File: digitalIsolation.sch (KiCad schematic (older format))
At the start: 6 parts, among them U14 74AHC1G14, U15 Si8651

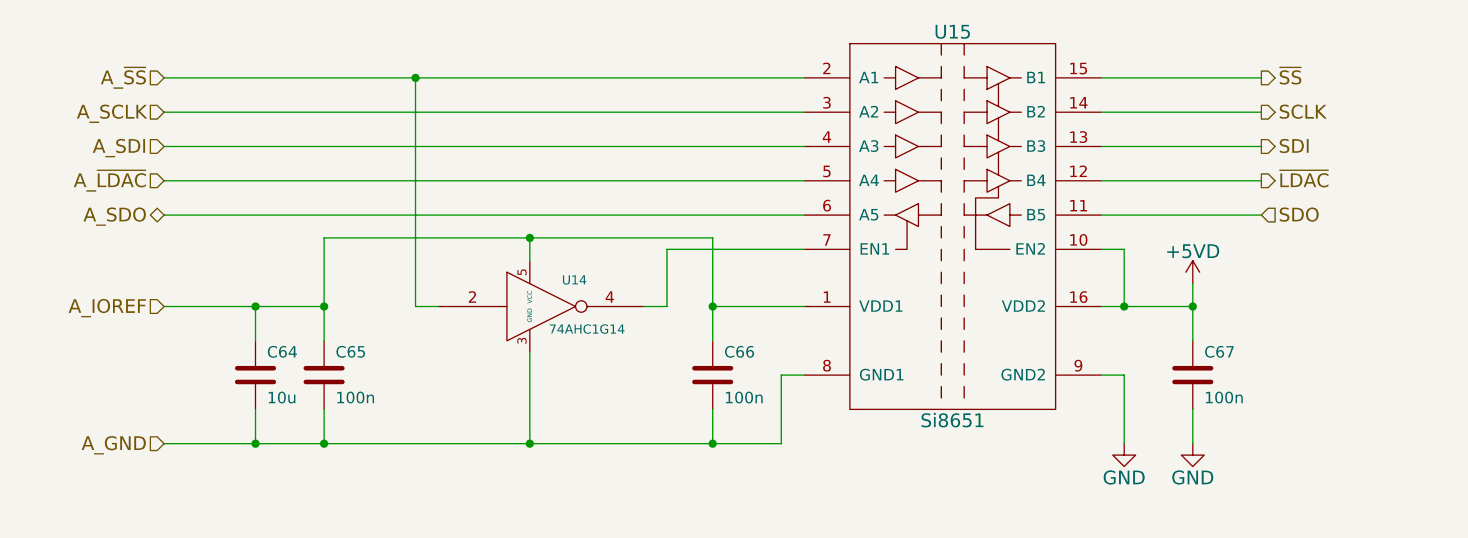
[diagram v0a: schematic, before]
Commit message: Updated all part descriptions
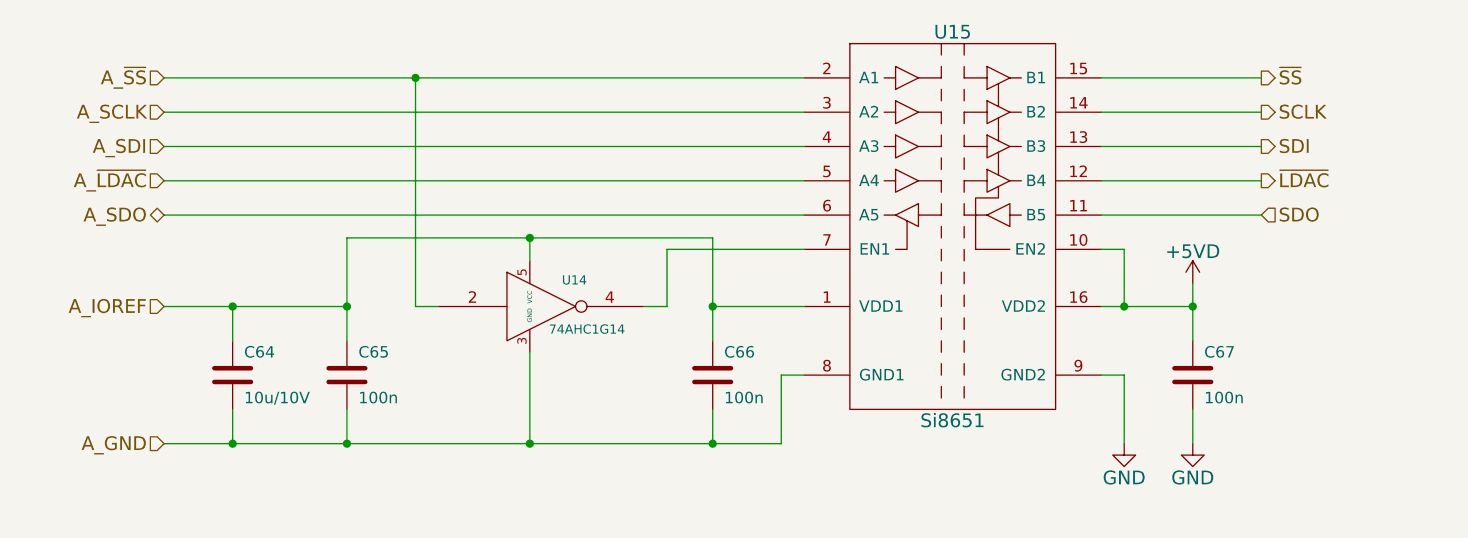
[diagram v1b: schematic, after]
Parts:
- C64: value 10u -> 10u/10V; Alt. Order Code (none) -> 81-GRM21BR61A106KE19; Alt. Supplier (none) -> Mouser; Note (none) -> 10μ/10V X5R 0805 ceramic capacitor; Package (none) -> 0805; Supplier (none) -> Farnell
- C65, C66, C67: Alt. Order Code (none) -> 710-885012206095; Alt. Supplier (none) -> Mouser; Note (none) -> 100n/50V X7R 0603 ceramic capacitor; Package (none) -> 0603; Supplier (none) -> Farnell
- U14: Alt. Order Code (none) -> 595-SN74AHC1G14DCKR; Alt. Supplier (none) -> Mouser; Note (none) -> Single Schmitt trigger inverter; Package (none) -> SC-70-5; Supplier (none) -> Farnell
- U15: Alt. Order Code (none) -> 634-SI8651EC-B-IS1; Alt. Supplier (none) -> Mouser; Note (none) -> Digital isolators 5 channel 3.75kV 8ns 4/1; Package (none) -> SOIC-16; Supplier (none) -> Farnell
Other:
- moved on the sheet: C64, C65
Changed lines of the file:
@@
 EESchema Schematic File Version 2
-LIBS:MicroFLiC_DAC_1_0-rescue
 LIBS:power
 LIBS:device
@@
 LIBS:valves
 LIBS:jakub
-LIBS:MicroFLiC_DAC_1_0-cache
+LIBS:MicroFLiC_DAC-cache
 EELAYER 25 0
 EELAYER END
@@
 F 4 "SI8651EC-B-IS1" H 7050 2850 60  0001 C CNN "Part Number"
 F 5 "Silicon Labs" H 7050 2850 60  0001 C CNN "Manufacturer"
-F 6 "2423323" H 7050 2850 60  0001 C CNN "Order Code"
+F 6 "SOIC-16" H 7050 2850 60  0001 C CNN "Package"
+F 7 "Farnell" H 7050 2850 60  0001 C CNN "Supplier"
+F 8 "2423323" H 7050 2850 60  0001 C CNN "Order Code"
+F 9 "Mouser" H 7050 2850 60  0001 C CNN "Alt. Supplier"
+F 10 "634-SI8651EC-B-IS1" H 7050 2850 60  0001 C CNN "Alt. Order Code"
+F 11 "Digital isolators 5 channel 3.75kV 8ns 4/1" H 7050 2850 60  0001 C CNN "Note"
 	1    7050 2850
 	1    0    0    -1
@@
 F 4 "MC0603B104K500CT" H 5300 7000 60  0001 C CNN "Part Number"
 F 5 "Multicomp" H 5300 7000 60  0001 C CNN "Manufacturer"
-F 6 "1759122" H 5300 7000 60  0001 C CNN "Order Code"
+F 6 "0603" H 8100 3500 60  0001 C CNN "Package"
+F 7 "Farnell" H 8100 3500 60  0001 C CNN "Supplier"
+F 8 "1759122" H 5300 7000 60  0001 C CNN "Order Code"
+F 9 "Mouser" H 8100 3500 60  0001 C CNN "Alt. Supplier"
+F 10 "710-885012206095" H 8100 3500 60  0001 C CNN "Alt. Order Code"
+F 11 "100n/50V X7R 0603 ceramic capacitor" H 8100 3500 60  0001 C CNN "Note"
 	1    8100 3500
 	1    0    0    -1
@@
 F 4 "SN74AHC1G14DCKR" H 5250 3200 60  0001 C CNN "Part Number"
 F 5 "Texas Instruments" H 5250 3200 60  0001 C CNN "Manufacturer"
-F 6 "1287468" H 5250 3200 60  0001 C CNN "Order Code"
+F 6 "SC-70-5" H 5250 3200 60  0001 C CNN "Package"
+F 7 "Farnell" H 5250 3200 60  0001 C CNN "Supplier"
+F 8 "1287468" H 5250 3200 60  0001 C CNN "Order Code"
+F 9 "Mouser" H 5250 3200 60  0001 C CNN "Alt. Supplier"
+F 10 "595-SN74AHC1G14DCKR" H 5250 3200 60  0001 C CNN "Alt. Order Code"
+F 11 "Single Schmitt trigger inverter" H 5250 3200 60  0001 C CNN "Note"
 	1    5250 3200
 	1    0    0    -1
@@
 F 4 "MC0603B104K500CT" H 5300 7000 60  0001 C CNN "Part Number"
 F 5 "Multicomp" H 5300 7000 60  0001 C CNN "Manufacturer"
-F 6 "1759122" H 5300 7000 60  0001 C CNN "Order Code"
+F 6 "0603" H 6000 3500 60  0001 C CNN "Package"
+F 7 "Farnell" H 6000 3500 60  0001 C CNN "Supplier"
+F 8 "1759122" H 5300 7000 60  0001 C CNN "Order Code"
+F 9 "Mouser" H 6000 3500 60  0001 C CNN "Alt. Supplier"
+F 10 "710-885012206095" H 6000 3500 60  0001 C CNN "Alt. Order Code"
+F 11 "100n/50V X7R 0603 ceramic capacitor" H 6000 3500 60  0001 C CNN "Note"
 	1    6000 3500
 	1    0    0    -1
@@
 L C C65
 U 1 1 5574AD7F
-P 4300 3500
+P 4400 3500
 AR Path="/5574AD7F" Ref="C65"  Part="1"
 AR Path="/5574A638/5574AD7F" Ref="C65"  Part="1"
-F 0 "C65" H 4350 3600 50  0000 L CNN
-F 1 "100n" H 4350 3400 50  0000 L CNN
-F 2 "Capacitors_SMD:C_0603" H 4338 3350 30  0001 C CNN
-F 3 "" H 4300 3500 60  0000 C CNN
-F 4 "MC0603B104K500CT" H 5300 7000 60  0001 C CNN "Part Number"
-F 5 "Multicomp" H 5300 7000 60  0001 C CNN "Manufacturer"
-F 6 "1759122" H 5300 7000 60  0001 C CNN "Order Code"
-	1    4300 3500
+F 0 "C65" H 4450 3600 50  0000 L CNN
+F 1 "100n" H 4450 3400 50  0000 L CNN
+F 2 "Capacitors_SMD:C_0603" H 4438 3350 30  0001 C CNN
+F 3 "" H 4400 3500 60  0000 C CNN
+F 4 "MC0603B104K500CT" H 5400 7000 60  0001 C CNN "Part Number"
+F 5 "Multicomp" H 5400 7000 60  0001 C CNN "Manufacturer"
+F 6 "0603" H 4400 3500 60  0001 C CNN "Package"
+F 7 "Farnell" H 4400 3500 60  0001 C CNN "Supplier"
+F 8 "1759122" H 5400 7000 60  0001 C CNN "Order Code"
+F 9 "Mouser" H 4400 3500 60  0001 C CNN "Alt. Supplier"
+F 10 "710-885012206095" H 4400 3500 60  0001 C CNN "Alt. Order Code"
+F 11 "100n/50V X7R 0603 ceramic capacitor" H 4400 3500 60  0001 C CNN "Note"
+	1    4400 3500
 	1    0    0    -1
 $EndComp
@@
 	5800 3200 5700 3200
 Wire Wire Line
-	4300 2900 6000 2900
+	4400 2900 6000 2900
 Wire Wire Line
 	5200 2900 5200 3000
 Wire Wire Line
-	4300 2900 4300 3350
+	4400 2900 4400 3350
 Connection ~ 5200 2900
 Wire Wire Line
-	4300 3650 4300 3800
+	4400 3650 4400 3800
 Wire Wire Line
 	6300 3800 3600 3800
@@
 Connection ~ 4700 2200
 Wire Wire Line
-	3600 3200 4300 3200
-Connection ~ 4300 3200
-Connection ~ 4300 3800
+	3600 3200 4400 3200
+Connection ~ 4400 3200
+Connection ~ 4400 3800
 Text HLabel 3600 2200 0    60   Input ~ 0
 A_~SS
@@
 L C C64
 U 1 1 5574B7E4
-P 4000 3500
+P 3900 3500
 AR Path="/5574B7E4" Ref="C64"  Part="1"
 AR Path="/5574A638/5574B7E4" Ref="C64"  Part="1"
-F 0 "C64" H 4050 3600 50  0000 L CNN
-F 1 "10u" H 4050 3400 50  0000 L CNN
-F 2 "Capacitors_SMD:C_0805" H 4038 3350 30  0001 C CNN
-F 3 "" H 4000 3500 60  0000 C CNN
-F 4 "GRM21BR61A106KE19L" H 4000 3500 60  0001 C CNN "Part Number"
-F 5 "Murata" H 4000 3500 60  0001 C CNN "Manufacturer"
-F 6 "1828805" H 4000 3500 60  0001 C CNN "Order Code"
-	1    4000 3500
-	1    0    0    -1
-$EndComp
-Wire Wire Line
-	4000 3350 4000 3200
-Connection ~ 4000 3200
-Wire Wire Line
-	4000 3650 4000 3800
-Connection ~ 4000 3800
+F 0 "C64" H 3950 3600 50  0000 L CNN
+F 1 "10u/10V" H 3950 3400 50  0000 L CNN
+F 2 "Capacitors_SMD:C_0805" H 3938 3350 30  0001 C CNN
+F 3 "" H 3900 3500 60  0000 C CNN
+F 4 "GRM21BR61A106KE19L" H 3900 3500 60  0001 C CNN "Part Number"
+F 5 "Murata" H 3900 3500 60  0001 C CNN "Manufacturer"
+F 6 "0805" H 3900 3500 60  0001 C CNN "Package"
+F 7 "Farnell" H 3900 3500 60  0001 C CNN "Supplier"
+F 8 "1828805" H 3900 3500 60  0001 C CNN "Order Code"
+F 9 "Mouser" H 3900 3500 60  0001 C CNN "Alt. Supplier"
+F 10 "81-GRM21BR61A106KE19" H 3900 3500 60  0001 C CNN "Alt. Order Code"
+F 11 "10μ/10V X5R 0805 ceramic capacitor" H 3900 3500 60  0001 C CNN "Note"
+	1    3900 3500
+	1    0    0    -1
+$EndComp
+Wire Wire Line
+	3900 3350 3900 3200
+Connection ~ 3900 3200
+Wire Wire Line
+	3900 3650 3900 3800
+Connection ~ 3900 3800
 $EndSCHEMATC

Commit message: Fixed LM3880 pull-up resistors to 5V
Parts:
- U14: Alt. Order Code 595-SN74AHC1G14DCKR -> 595-SN74AHC1G14DBVR; Order Code 1287468 -> 1105919; Package SC-70-5 -> SOT-23-5; Part Number SN74AHC1G14DCKR -> SN74AHC1G14DBVR
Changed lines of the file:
@@
 Connection ~ 7800 3200
 $Comp
-L +5VD #PWR083
+L +5VD #PWR087
 U 1 1 5574AC36
 P 8100 3100
-F 0 "#PWR083" H 8100 2950 60  0001 C CNN
+F 0 "#PWR087" H 8100 2950 60  0001 C CNN
 F 1 "+5VD" H 8100 3240 60  0000 C CNN
 F 2 "" H 8100 3100 60  0000 C CNN
@@
 	8100 3650 8100 3800
 $Comp
-L GND #PWR084
+L GND #PWR088
 U 1 1 5574AC81
 P 7800 3800
-F 0 "#PWR084" H 7800 3550 60  0001 C CNN
+F 0 "#PWR088" H 7800 3550 60  0001 C CNN
 F 1 "GND" H 7800 3650 60  0000 C CNN
 F 2 "" H 7800 3800 60  0000 C CNN
@@
 $EndComp
 $Comp
-L GND #PWR085
+L GND #PWR089
 U 1 1 5574ACAE
 P 8100 3800
-F 0 "#PWR085" H 8100 3550 60  0001 C CNN
+F 0 "#PWR089" H 8100 3550 60  0001 C CNN
 F 1 "GND" H 8100 3650 60  0000 C CNN
 F 2 "" H 8100 3800 60  0000 C CNN
@@
 F 2 "Housings_SOT-23_SOT-143_TSOT-6:SOT-23-5" H 5345 3065 30  0001 C CNN
 F 3 "" H 5395 3315 60  0000 C CNN
-F 4 "SN74AHC1G14DCKR" H 5250 3200 60  0001 C CNN "Part Number"
+F 4 "SN74AHC1G14DBVR" H 5250 3200 60  0001 C CNN "Part Number"
 F 5 "Texas Instruments" H 5250 3200 60  0001 C CNN "Manufacturer"
-F 6 "SC-70-5" H 5250 3200 60  0001 C CNN "Package"
+F 6 "SOT-23-5" H 5250 3200 60  0001 C CNN "Package"
 F 7 "Farnell" H 5250 3200 60  0001 C CNN "Supplier"
-F 8 "1287468" H 5250 3200 60  0001 C CNN "Order Code"
+F 8 "1105919" H 5250 3200 60  0001 C CNN "Order Code"
 F 9 "Mouser" H 5250 3200 60  0001 C CNN "Alt. Supplier"
-F 10 "595-SN74AHC1G14DCKR" H 5250 3200 60  0001 C CNN "Alt. Order Code"
+F 10 "595-SN74AHC1G14DBVR" H 5250 3200 60  0001 C CNN "Alt. Order Code"
 F 11 "Single Schmitt trigger inverter" H 5250 3200 60  0001 C CNN "Note"
 	1    5250 3200

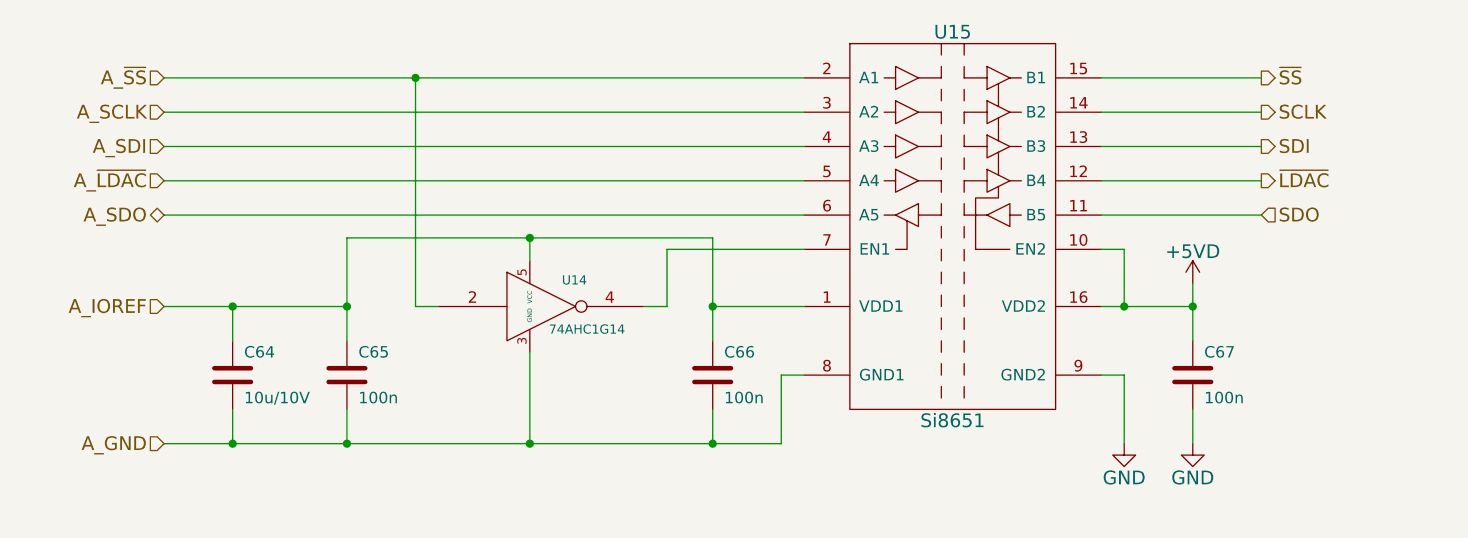
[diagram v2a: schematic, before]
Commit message: Fixed ground problems, added bypass capacitors, added resistor between digital isolator and DAC
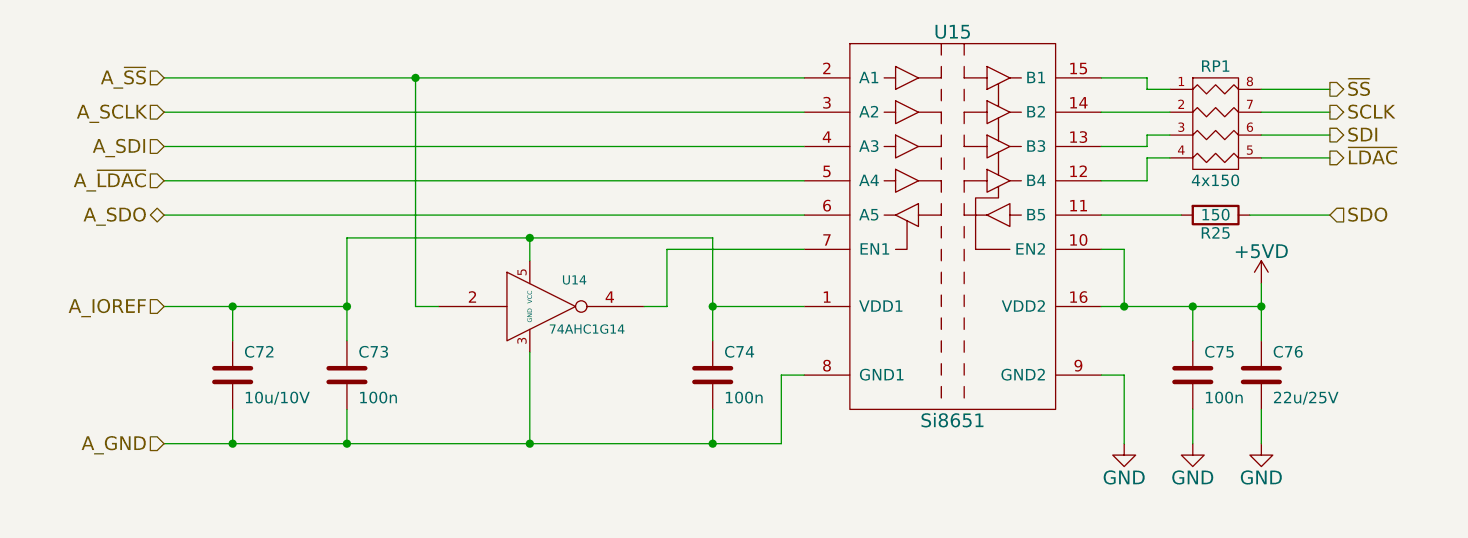
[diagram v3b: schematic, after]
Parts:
- added C76: 22u/25V, Capacitors_SMD:C_1210, symbol C
- added R25: 150, Resistors_SMD:R_0805, symbol R
- added RP1: 4x150, Resistors_SMD:R_Array_Convex_4x0603, symbol R_PACK4
- renumbered C64 to C72, C65 to C73, C66 to C74, C67 to C75
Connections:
- net +5VD: now also C76.1
- net GND: now also C76.2
- net SCLK: now also RP1.7 (R2); no longer U15.14 (B2)
- net SDI: now also RP1.6 (R3); no longer U15.13 (B3)
- net SDO: now also R25.1; no longer U15.11 (B5)
- net ~LDAC: now also RP1.5 (R4); no longer U15.12 (B4)
- net ~SS: now also RP1.8 (R1); no longer U15.15 (B1)
- new net: R25.2, U15.11 (B5)
- new net: RP1.4 (P4), U15.12 (B4)
- new net: RP1.3 (P3), U15.13 (B3)
- new net: RP1.2 (P2), U15.14 (B2)
- new net: RP1.1 (P1), U15.15 (B1)
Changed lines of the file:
@@
 Comment4 ""
 $EndDescr
-Text HLabel 8400 2200 2    60   Output ~ 0
+Text HLabel 8700 2250 2    60   Output ~ 0
 ~SS
-Text HLabel 8400 2350 2    60   Output ~ 0
+Text HLabel 8700 2350 2    60   Output ~ 0
 SCLK
-Text HLabel 8400 2500 2    60   Output ~ 0
+Text HLabel 8700 2450 2    60   Output ~ 0
 SDI
-Text HLabel 8400 2800 2    60   Input ~ 0
+Text HLabel 8700 2800 2    60   Input ~ 0
 SDO
-Text HLabel 8400 2650 2    60   Output ~ 0
+Text HLabel 8700 2550 2    60   Output ~ 0
 ~LDAC
 $Comp
@@
 $EndComp
 Wire Wire Line
-	7700 2200 8400 2200
-Wire Wire Line
-	8400 2350 7700 2350
-Wire Wire Line
-	7700 2500 8400 2500
-Wire Wire Line
-	8400 2650 7700 2650
-Wire Wire Line
-	7700 2800 8400 2800
+	8000 2350 7700 2350
+Wire Wire Line
+	7700 2800 8050 2800
 Wire Wire Line
 	7700 2950 7800 2950
@@
 	7800 2950 7800 3200
 Wire Wire Line
-	7700 3200 8100 3200
-$Comp
-L C C67
+	7700 3200 8400 3200
+$Comp
+L C C75
 U 1 1 5574AB6E
 P 8100 3500
-AR Path="/5574AB6E" Ref="C67"  Part="1"
-AR Path="/5574A638/5574AB6E" Ref="C67"  Part="1"
-F 0 "C67" H 8150 3600 50  0000 L CNN
+F 0 "C75" H 8150 3600 50  0000 L CNN
 F 1 "100n" H 8150 3400 50  0000 L CNN
 F 2 "Capacitors_SMD:C_0603" H 8138 3350 30  0001 C CNN
@@
 $EndComp
 Wire Wire Line
-	8100 3100 8100 3350
+	8100 3200 8100 3350
 Connection ~ 7800 3200
-$Comp
-L +5VD #PWR087
-U 1 1 5574AC36
-P 8100 3100
-F 0 "#PWR087" H 8100 2950 60  0001 C CNN
-F 1 "+5VD" H 8100 3240 60  0000 C CNN
-F 2 "" H 8100 3100 60  0000 C CNN
-F 3 "" H 8100 3100 60  0000 C CNN
-	1    8100 3100
-	1    0    0    -1
-$EndComp
 Connection ~ 8100 3200
 Wire Wire Line
@@
 	8100 3650 8100 3800
 $Comp
-L GND #PWR088
+L GND #PWR084
 U 1 1 5574AC81
 P 7800 3800
-F 0 "#PWR088" H 7800 3550 60  0001 C CNN
+F 0 "#PWR084" H 7800 3550 60  0001 C CNN
 F 1 "GND" H 7800 3650 60  0000 C CNN
 F 2 "" H 7800 3800 60  0000 C CNN
@@
 $EndComp
 $Comp
-L GND #PWR089
+L GND #PWR085
 U 1 1 5574ACAE
 P 8100 3800
-F 0 "#PWR089" H 8100 3550 60  0001 C CNN
+F 0 "#PWR085" H 8100 3550 60  0001 C CNN
 F 1 "GND" H 8100 3650 60  0000 C CNN
 F 2 "" H 8100 3800 60  0000 C CNN
@@
 $EndComp
 $Comp
-L C C66
+L C C74
 U 1 1 5574AE37
 P 6000 3500
-AR Path="/5574AE37" Ref="C66"  Part="1"
-AR Path="/5574A638/5574AE37" Ref="C66"  Part="1"
-F 0 "C66" H 6050 3600 50  0000 L CNN
+F 0 "C74" H 6050 3600 50  0000 L CNN
 F 1 "100n" H 6050 3400 50  0000 L CNN
 F 2 "Capacitors_SMD:C_0603" H 6038 3350 30  0001 C CNN
@@
 	6300 3500 6300 3800
 $Comp
-L C C65
+L C C73
 U 1 1 5574AD7F
 P 4400 3500
-AR Path="/5574AD7F" Ref="C65"  Part="1"
-AR Path="/5574A638/5574AD7F" Ref="C65"  Part="1"
-F 0 "C65" H 4450 3600 50  0000 L CNN
+F 0 "C73" H 4450 3600 50  0000 L CNN
 F 1 "100n" H 4450 3400 50  0000 L CNN
 F 2 "Capacitors_SMD:C_0603" H 4438 3350 30  0001 C CNN
@@
 A_GND
 $Comp
-L C C64
+L C C72
 U 1 1 5574B7E4
 P 3900 3500
-AR Path="/5574B7E4" Ref="C64"  Part="1"
-AR Path="/5574A638/5574B7E4" Ref="C64"  Part="1"
-F 0 "C64" H 3950 3600 50  0000 L CNN
+F 0 "C72" H 3950 3600 50  0000 L CNN
 F 1 "10u/10V" H 3950 3400 50  0000 L CNN
 F 2 "Capacitors_SMD:C_0805" H 3938 3350 30  0001 C CNN
@@
 	3900 3650 3900 3800
 Connection ~ 3900 3800
+$Comp
+L R R25
+U 1 1 56E0FC32
+P 8200 2800
+F 0 "R25" V 8280 2800 50  0000 C CNN
+F 1 "150" V 8200 2800 50  0000 C CNN
+F 2 "Resistors_SMD:R_0805" V 8130 2800 50  0001 C CNN
+F 3 "" H 8200 2800 50  0000 C CNN
+F 4 "MCWR08X1500FTL" H 8200 2800 60  0001 C CNN "Part Number"
+F 5 "Multicomp" H 8200 2800 60  0001 C CNN "Manufacturer"
+F 6 "0805" H 8200 2800 60  0001 C CNN "Package"
+F 7 "Farnell" H 8200 2800 60  0001 C CNN "Supplier"
+F 8 "2447574" H 8200 2800 60  0001 C CNN "Order Code"
+F 9 "Mouser" H 8200 2800 60  0001 C CNN "Alt. Supplier"
+F 10 "71-TNPW0805150RFEEA" H 8200 2800 60  0001 C CNN "Alt. Order Code"
+F 11 "150Ω/1% 0805 resistor" H 8200 2800 60  0001 C CNN "Note"
+	1    8200 2800
+	0    1    1    0
+$EndComp
+Wire Wire Line
+	8400 2250 8700 2250
+Wire Wire Line
+	8400 2350 8700 2350
+Wire Wire Line
+	8400 2450 8700 2450
+Wire Wire Line
+	8400 2550 8700 2550
+Wire Wire Line
+	8350 2800 8700 2800
+$Comp
+L R_PACK4 RP1
+U 1 1 56E10B8D
+P 8200 2600
+F 0 "RP1" H 8200 3050 50  0000 C CNN
+F 1 "4x150" H 8200 2550 50  0000 C CNN
+F 2 "Resistors_SMD:R_Array_Convex_4x0603" H 8200 2600 50  0001 C CNN
+F 3 "" H 8200 2600 50  0000 C CNN
+F 4 "YC164-JR-07150RL" H 8200 2600 60  0001 C CNN "Part Number"
+F 5 "Yageo" H 8200 2600 60  0001 C CNN "Manufacturer"
+F 6 "4×0603" H 8200 2600 60  0001 C CNN "Package"
+F 7 "Farnell" H 8200 2600 60  0001 C CNN "Supplier"
+F 8 "9234462" H 8200 2600 60  0001 C CNN "Order Code"
+F 9 "Mouser" H 8200 2600 60  0001 C CNN "Alt. Supplier"
+F 10 "603-YC164-JR-07150RL" H 8200 2600 60  0001 C CNN "Alt. Order Code"
+F 11 "4×150Ω/5% 0603 resistor array" H 8200 2600 60  0001 C CNN "Note"
+	1    8200 2600
+	1    0    0    -1
+$EndComp
+Wire Wire Line
+	7700 2200 7900 2200
+Wire Wire Line
+	7900 2200 7900 2250
+Wire Wire Line
+	7900 2250 8000 2250
+Wire Wire Line
+	8000 2450 7900 2450
+Wire Wire Line
+	7900 2450 7900 2500
+Wire Wire Line
+	7900 2500 7700 2500
+Wire Wire Line
+	7700 2650 7900 2650
+Wire Wire Line
+	7900 2650 7900 2550
+Wire Wire Line
+	7900 2550 8000 2550
+$Comp
+L C C76
+U 1 1 56E16574
+P 8400 3500
+F 0 "C76" H 8450 3600 50  0000 L CNN
+F 1 "22u/25V" H 8450 3400 50  0000 L CNN
+F 2 "Capacitors_SMD:C_1210" H 8438 3350 30  0001 C CNN
+F 3 "" H 8400 3500 60  0000 C CNN
+F 4 "GRM32ER61E226ME15L" H 8400 3500 60  0001 C CNN "Part Number"
+F 5 "Murata" H 8400 3500 60  0001 C CNN "Manufacturer"
+F 6 "1210" H 8400 3500 60  0001 C CNN "Package"
+F 7 "Farnell" H 8400 3500 60  0001 C CNN "Supplier"
+F 8 "1735539" H 8400 3500 60  0001 C CNN "Order Code"
+F 9 "Mouser" H 8400 3500 60  0001 C CNN "Alt. Supplier"
+F 10 "81-GRM32ER61E226ME5L" H 8400 3500 60  0001 C CNN "Alt. Order Code"
+F 11 "22μF/25V X5R 1210 ceramic capacitor" H 8400 3500 60  0001 C CNN "Note"
+	1    8400 3500
+	1    0    0    -1
+$EndComp
+Wire Wire Line
+	8400 3100 8400 3350
+Connection ~ 8400 3200
+$Comp
+L +5VD #PWR086
+U 1 1 5574AC36
+P 8400 3100
+F 0 "#PWR086" H 8400 2950 60  0001 C CNN
+F 1 "+5VD" H 8400 3240 60  0000 C CNN
+F 2 "" H 8400 3100 60  0000 C CNN
+F 3 "" H 8400 3100 60  0000 C CNN
+	1    8400 3100
+	1    0    0    -1
+$EndComp
+Wire Wire Line
+	8400 3650 8400 3800
+$Comp
+L GND #PWR087
+U 1 1 56E16784
+P 8400 3800
+F 0 "#PWR087" H 8400 3550 60  0001 C CNN
+F 1 "GND" H 8400 3650 60  0000 C CNN
+F 2 "" H 8400 3800 60  0000 C CNN
+F 3 "" H 8400 3800 60  0000 C CNN
+	1    8400 3800
+	1    0    0    -1
+$EndComp
 $EndSCHEMATC
